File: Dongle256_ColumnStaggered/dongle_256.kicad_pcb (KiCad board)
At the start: 2 copper layers, 138.1 x 116 mm, 67 parts, among them J1 Conn_01x02_Male, J2 Conn_01x02_Male, SW1 GateronLP, SW10 GateronLP, SW11 GateronLP, SW12 GateronLP, SW13 GateronLP, SW14 GateronLP, SW15 GateronLP, SW16 GateronLP, SW17 GateronLP, SW18 GateronLP, SW19 GateronLP, SW2 GateronLP, SW20 GateronLP, SW21 GateronLP, SW22 GateronLP, SW23 GateronLP, SW24 GateronLP, SW25 GateronLP, SW26 GateronLP, SW27 GateronLP, SW28 GateronLP, SW29 GateronLP, SW3 GateronLP, SW30 GateronLP, SW31 SW_DIP_x03, SW4 GateronLP, SW5 GateronLP, SW6 GateronLP, SW7 GateronLP, SW8 GateronLP, SW9 GateronLP, U1 NRF52840-DONGLE, U2 NRF52840-DONGLE

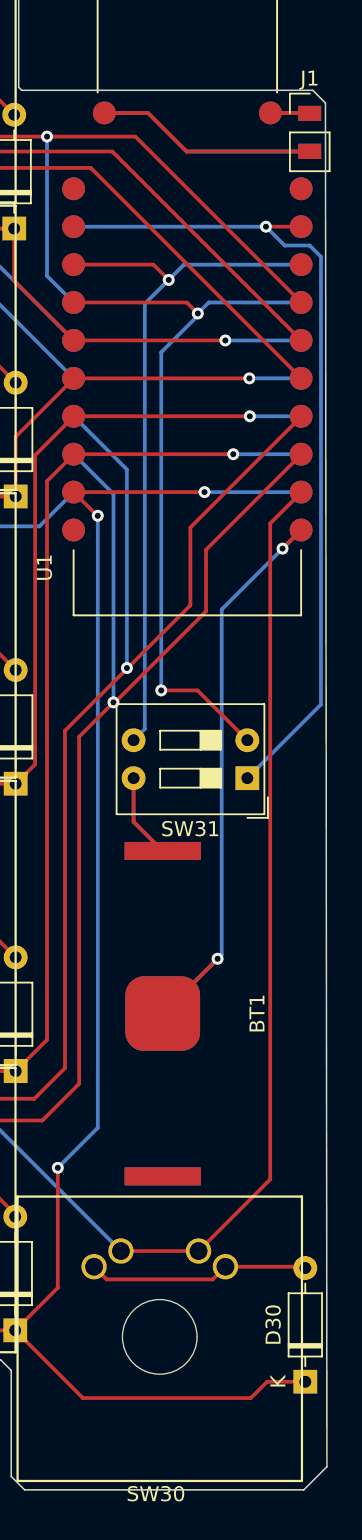
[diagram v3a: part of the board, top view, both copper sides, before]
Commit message: Move battery holder of columnStaggered PCB up away from thumb key
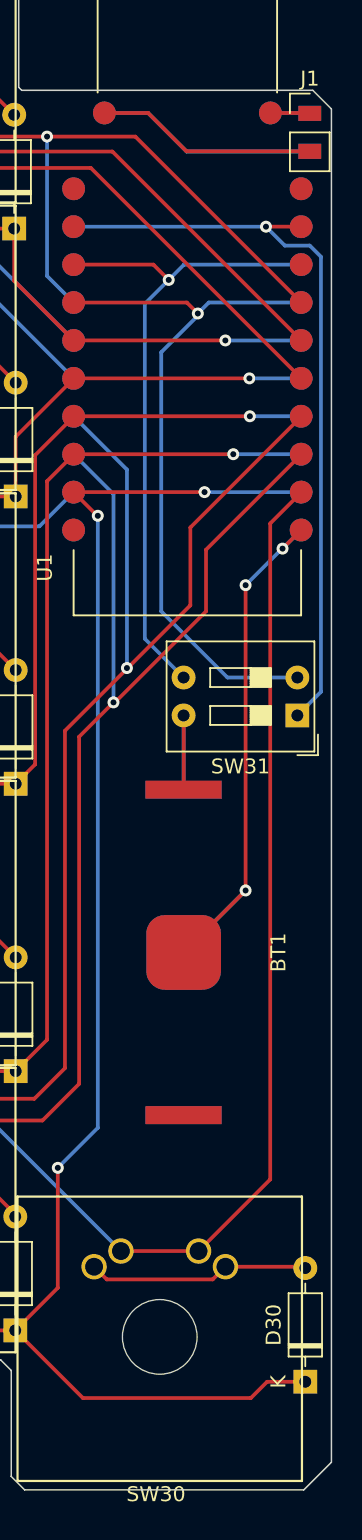
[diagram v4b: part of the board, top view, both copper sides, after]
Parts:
- moved SW31 5.37 mm to (163.8, 95.2)
- moved BT1 4.33 mm to (156.2, 111.0)
- moved BT2 4.33 mm to (156.2, 111.0)
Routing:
- net Net-(U1-PadOUT): track 56.7 -> 51.1 mm
- net Net-(BT1-Pad2): track 43.2 -> 39.2 mm, vias 2 -> 3
- net Net-(U1-Pad0.17): track 47.9 -> 44.5 mm
- net Net-(SW31-Pad2): track 49.3 -> 47.8 mm, vias 2 -> 1
- net Net-(BT1-Pad1): track 11.4 -> 9.95 mm
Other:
- board size 138.1 x 116 mm -> 138.4 x 116 mm
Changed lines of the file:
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@@
   )
   (footprint "MVB:TBH-CR2032-M04" (layer "F.Cu")
-    (at 154.75 115.15 90)
+    (at 156.15 111.05 90)
     (property "Sheetfile" "File: dongle_256.kicad_sch")
     (property "Sheetname" "")
@@
   )
   (footprint "Button_Switch_THT:SW_DIP_SPSTx02_Slide_9.78x7.26mm_W7.62mm_P2.54mm" (layer "F.Cu")
-    (at 160.4175 99.375 180)
+    (at 163.7675 95.175 180)
     (descr "2x-dip-switch SPST , Slide, row spacing 7.62 mm (300 mils), body size 9.78x7.26mm (see e.g. https://www.ctscorp.com/wp-content/uploads/206-208.pdf)")
     (tags "DIP Switch SPST Slide 7.62mm 300mil")
@@
   )
   (footprint "MVB:TBH-CR2032-M04" (layer "B.Cu")
-    (at 154.75 115.15 -90)
+    (at 156.15 111.05 -90)
     (property "Sheetfile" "File: dongle_256.kicad_sch")
     (property "Sheetname" "")
@@
   (gr_line (start 27.7 42.85) (end 29.15 41.4) (layer "Edge.Cuts") (width 0.1))
   (gr_line (start 87 36.15) (end 87 31.45) (layer "Edge.Cuts") (width 0.1))
-  (gr_line (start 165.65 54.15) (end 165.75 145.5) (layer "Edge.Cuts") (width 0.1))
   (gr_line (start 106.45 36.25) (end 106.8 36.6) (layer "Edge.Cuts") (width 0.1))
   (gr_line (start 29.15 41.4) (end 67.1 41.4) (layer "Edge.Cuts") (width 0.1))
   (gr_line (start 125.3 36.6) (end 125.75 37.05) (layer "Edge.Cuts") (width 0.1))
-  (gr_line (start 165.75 145.5) (end 164.2 147.05) (layer "Edge.Cuts") (width 0.1))
+  (gr_line (start 166.05 145.2) (end 164.2 147.05) (layer "Edge.Cuts") (width 0.1))
   (gr_line (start 144.6 146.15) (end 144.6 139.05) (layer "Edge.Cuts") (width 0.1))
   (gr_line (start 125.75 37.05) (end 125.75 41.2) (layer "Edge.Cuts") (width 0.1))
@@
   (gr_line (start 125.75 41.2) (end 126.1 41.55) (layer "Edge.Cuts") (width 0.1))
   (gr_line (start 106.8 36.6) (end 125.3 36.6) (layer "Edge.Cuts") (width 0.1))
-  (gr_line (start 164.8 53.3) (end 165.65 54.15) (layer "Edge.Cuts") (width 0.1))
+  (gr_line (start 164.8 53.3) (end 166.05 54.55) (layer "Edge.Cuts") (width 0.1))
   (gr_line (start 145.3 53.3) (end 145.1 53.1) (layer "Edge.Cuts") (width 0.1))
   (gr_line (start 48.95 138.35) (end 27.7 117.1) (layer "Edge.Cuts") (width 0.1))
@@
   (gr_line (start 106.45 31.5) (end 106.45 36.25) (layer "Edge.Cuts") (width 0.1))
   (gr_line (start 67.1 41.4) (end 67.5 41) (layer "Edge.Cuts") (width 0.1))
+  (gr_line (start 166.05 145.2) (end 166.05 54.55) (layer "Edge.Cuts") (width 0.1))
   (gr_line (start 67.5 37) (end 67.9 36.6) (layer "Edge.Cuts") (width 0.1))
   (gr_line (start 145.5 147.05) (end 144.6 146.15) (layer "Edge.Cuts") (width 0.1))
@@
   (segment (start 137.97 83.93875) (end 137.97 86.17) (width 0.25) (layer "B.Cu") (net 41))
   (segment (start 139.2 106.85) (end 139.2 118.303) (width 0.25) (layer "B.Cu") (net 41))
+  (segment (start 160.3 86.45) (end 160.3 106.9) (width 0.25) (layer "F.Cu") (net 42))
+  (segment (start 156.15 111.05) (end 160.3 106.9) (width 0.25) (layer "F.Cu") (net 42))
   (segment (start 162.775 84) (end 164.02 82.755) (width 0.25) (layer "F.Cu") (net 42))
-  (segment (start 154.75 115.15) (end 158.425 111.475) (width 0.25) (layer "F.Cu") (net 42))
-  (via (at 158.425 111.475) (size 0.8) (drill 0.4) (layers "F.Cu" "B.Cu") (net 42))
+  (via (at 160.3 106.9) (size 0.8) (drill 0.4) (layers "F.Cu" "B.Cu") (net 42))
   (via (at 162.775 84) (size 0.8) (drill 0.4) (layers "F.Cu" "B.Cu") (net 42))
-  (segment (start 158.7 111.2) (end 158.425 111.475) (width 0.25) (layer "B.Cu") (net 42))
-  (segment (start 162.775 84) (end 158.7 88.075) (width 0.25) (layer "B.Cu") (net 42))
-  (segment (start 158.425 111.475) (end 154.75 115.15) (width 0.25) (layer "B.Cu") (net 42))
+  (via (at 160.3 86.45) (size 0.8) (drill 0.4) (layers "F.Cu" "B.Cu") (net 42))
+  (segment (start 162.75 84) (end 162.775 84) (width 0.25) (layer "B.Cu") (net 42))
+  (segment (start 156.15 111.05) (end 160.3 106.9) (width 0.25) (layer "B.Cu") (net 42))
+  (segment (start 160.3 86.45) (end 162.75 84) (width 0.25) (layer "B.Cu") (net 42))
   (segment (start 164.02 82.755) (end 162.775 84) (width 0.25) (layer "B.Cu") (net 42))
-  (segment (start 158.7 88.075) (end 158.7 111.2) (width 0.25) (layer "B.Cu") (net 42))
-  (segment (start 152.7975 102.2975) (end 154.75 104.25) (width 0.25) (layer "F.Cu") (net 45))
-  (segment (start 152.7975 99.375) (end 152.7975 102.2975) (width 0.25) (layer "F.Cu") (net 45))
-  (segment (start 152.7975 102.2975) (end 154.75 104.25) (width 0.25) (layer "B.Cu") (net 45))
-  (segment (start 152.7975 99.375) (end 152.7975 102.2975) (width 0.25) (layer "B.Cu") (net 45))
+  (segment (start 156.15 100.15) (end 156.15 95.1775) (width 0.25) (layer "F.Cu") (net 45))
+  (segment (start 156.15 95.1775) (end 156.1475 95.175) (width 0.25) (layer "F.Cu") (net 45))
+  (segment (start 156.15 100.15) (end 156.15 95.1775) (width 0.25) (layer "B.Cu") (net 45))
+  (segment (start 156.15 95.1775) (end 156.1475 95.175) (width 0.25) (layer "B.Cu") (net 45))
   (segment (start 164.585 54.815) (end 164.6 54.8) (width 0.25) (layer "F.Cu") (net 47))
   (segment (start 161.96 54.815) (end 164.565 54.815) (width 0.25) (layer "F.Cu") (net 47))
@@
   (via (at 161.665 62.435) (size 0.8) (drill 0.4) (layers "F.Cu" "B.Cu") (net 49))
   (segment (start 148.78 62.435) (end 161.665 62.435) (width 0.25) (layer "B.Cu") (net 49))
-  (segment (start 164.6 63.7) (end 162.93 63.7) (width 0.25) (layer "B.Cu") (net 49))
-  (segment (start 165.35 94.4425) (end 165.35 64.45) (width 0.25) (layer "B.Cu") (net 49))
-  (segment (start 165.35 64.45) (end 164.6 63.7) (width 0.25) (layer "B.Cu") (net 49))
-  (segment (start 160.4175 99.375) (end 165.35 94.4425) (width 0.25) (layer "B.Cu") (net 49))
+  (segment (start 163.7675 95.175) (end 165.35 93.5925) (width 0.25) (layer "B.Cu") (net 49))
   (segment (start 162.93 63.7) (end 161.665 62.435) (width 0.25) (layer "B.Cu") (net 49))
-  (segment (start 154.65 93.5) (end 157.0825 93.5) (width 0.25) (layer "F.Cu") (net 50))
+  (segment (start 165.35 64.45) (end 164.6 63.7) (width 0.25) (layer "B.Cu") (net 49))
+  (segment (start 164.6 63.7) (end 162.93 63.7) (width 0.25) (layer "B.Cu") (net 49))
+  (segment (start 165.35 93.5925) (end 165.35 64.45) (width 0.25) (layer "B.Cu") (net 49))
   (segment (start 156.365 67.515) (end 148.78 67.515) (width 0.25) (layer "F.Cu") (net 50))
-  (segment (start 157.0825 93.5) (end 160.4175 96.835) (width 0.25) (layer "F.Cu") (net 50))
   (segment (start 157.1 68.25) (end 156.365 67.515) (width 0.25) (layer "F.Cu") (net 50))
   (via (at 157.1 68.25) (size 0.8) (drill 0.4) (layers "F.Cu" "B.Cu") (net 50))
-  (via (at 154.65 93.5) (size 0.8) (drill 0.4) (layers "F.Cu" "B.Cu") (net 50))
-  (segment (start 154.65 70.85) (end 157.1 68.4) (width 0.25) (layer "B.Cu") (net 50))
-  (segment (start 154.65 93.5) (end 154.65 70.85) (width 0.25) (layer "B.Cu") (net 50))
+  (segment (start 157.1 68.4) (end 154.65 70.85) (width 0.25) (layer "B.Cu") (net 50))
+  (segment (start 159.085 92.635) (end 163.7675 92.635) (width 0.25) (layer "B.Cu") (net 50))
+  (segment (start 154.65 70.85) (end 154.65 88.2) (width 0.25) (layer "B.Cu") (net 50))
+  (segment (start 157.1 68.25) (end 157.1 68.4) (width 0.25) (layer "B.Cu") (net 50))
   (segment (start 157.835 67.515) (end 164.02 67.515) (width 0.25) (layer "B.Cu") (net 50))
   (segment (start 157.1 68.25) (end 157.835 67.515) (width 0.25) (layer "B.Cu") (net 50))
-  (segment (start 157.1 68.4) (end 157.1 68.25) (width 0.25) (layer "B.Cu") (net 50))
+  (segment (start 154.65 88.2) (end 159.085 92.635) (width 0.25) (layer "B.Cu") (net 50))
   (segment (start 154.125 64.975) (end 148.78 64.975) (width 0.25) (layer "F.Cu") (net 51))
   (segment (start 155.15 66) (end 154.125 64.975) (width 0.25) (layer "F.Cu") (net 51))
   (via (at 155.15 66) (size 0.8) (drill 0.4) (layers "F.Cu" "B.Cu") (net 51))
-  (segment (start 153.55 96.0825) (end 152.7975 96.835) (width 0.25) (layer "B.Cu") (net 51))
+  (segment (start 153.55 67.6) (end 153.55 90.0375) (width 0.25) (layer "B.Cu") (net 51))
+  (segment (start 153.55 90.0375) (end 156.1475 92.635) (width 0.25) (layer "B.Cu") (net 51))
   (segment (start 156.175 64.975) (end 164.02 64.975) (width 0.25) (layer "B.Cu") (net 51))
-  (segment (start 153.55 67.6) (end 153.55 96.0825) (width 0.25) (layer "B.Cu") (net 51))
   (segment (start 155.15 66) (end 153.55 67.6) (width 0.25) (layer "B.Cu") (net 51))
   (segment (start 155.15 66) (end 156.175 64.975) (width 0.25) (layer "B.Cu") (net 51))
